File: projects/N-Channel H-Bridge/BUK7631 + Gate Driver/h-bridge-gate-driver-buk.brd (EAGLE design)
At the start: 160 x 100 mm, 24 parts, among them IC1 MIC5014YM, IC2 MIC5014YM, IC3 MIC5014YM, IC4 MIC5014YM, Q1 BUK7631, Q2 BUK7631, Q3 BUK7631, Q4 BUK7631'

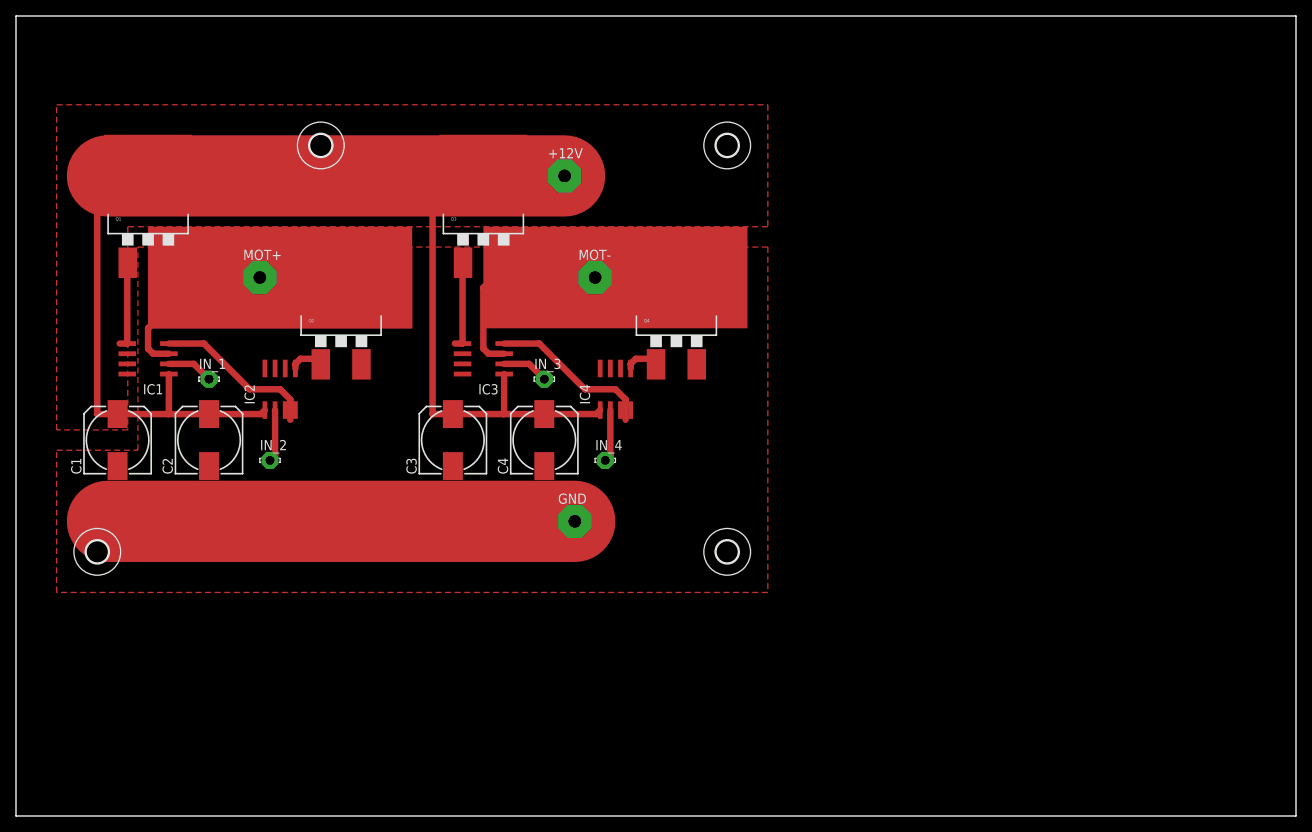
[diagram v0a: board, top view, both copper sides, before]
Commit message: smaller traces + images
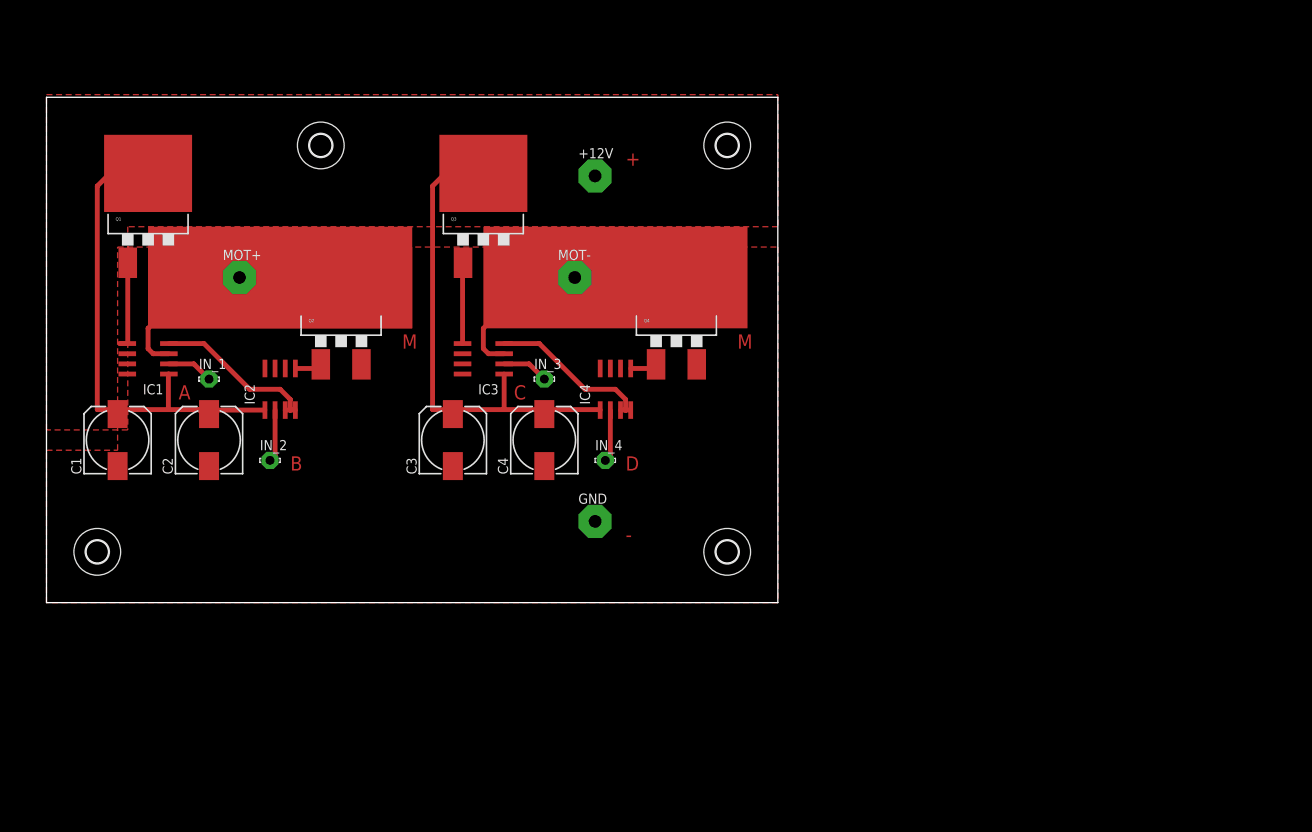
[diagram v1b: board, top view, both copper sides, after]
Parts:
- moved +12V 3.81 mm to (72.4, 80.0)
- moved GND 2.54 mm to (72.4, 36.8)
- moved MOT- 2.54 mm to (69.8, 67.3)
- moved MOT+ 2.54 mm to (27.9, 67.3)
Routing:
- net GND: track 99.6 -> 41.3 mm
- net VCC: track 174.1 -> 124.6 mm
- net N$4: track 11.1 -> 10.1 mm
- net MOT+: track 36.4 -> 37.1 mm
- net N$98: track 3.99 -> 3.39 mm
- net N$97: track 3.99 -> 3.39 mm
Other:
- board size 160 x 100 mm -> 91.4 x 63.2 mm
- board text added: "+"
- board text added: "-"
- board text added: "A"
- board text added: "B"
- board text added: "C"
- board text added: "D"
- board text added: "M"

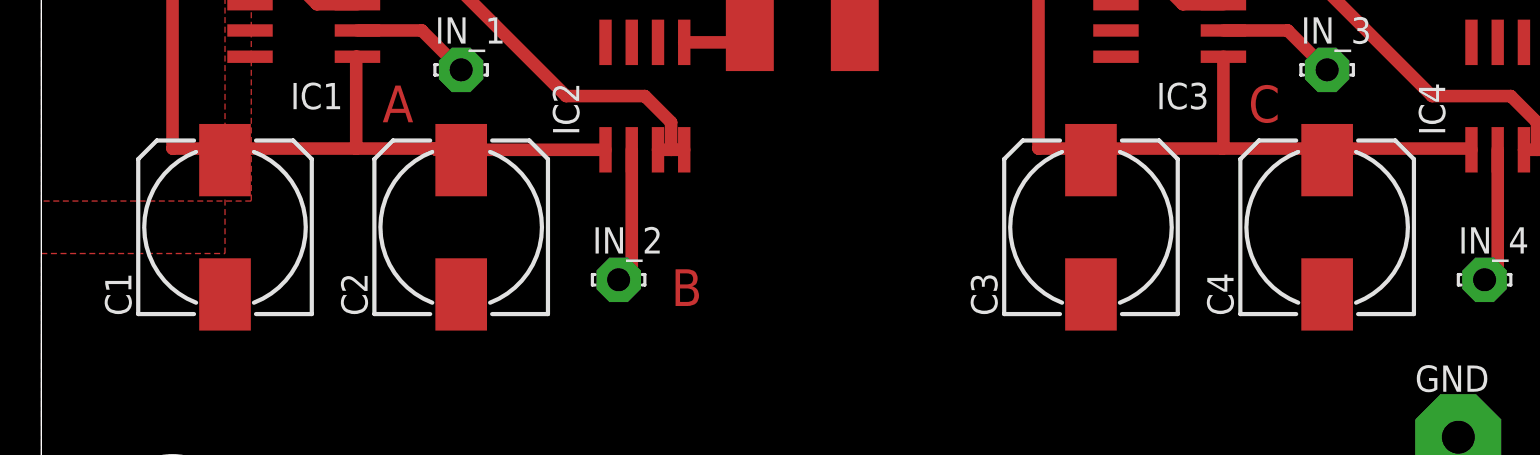
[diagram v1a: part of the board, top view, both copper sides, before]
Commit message: replaced with the proper cap package
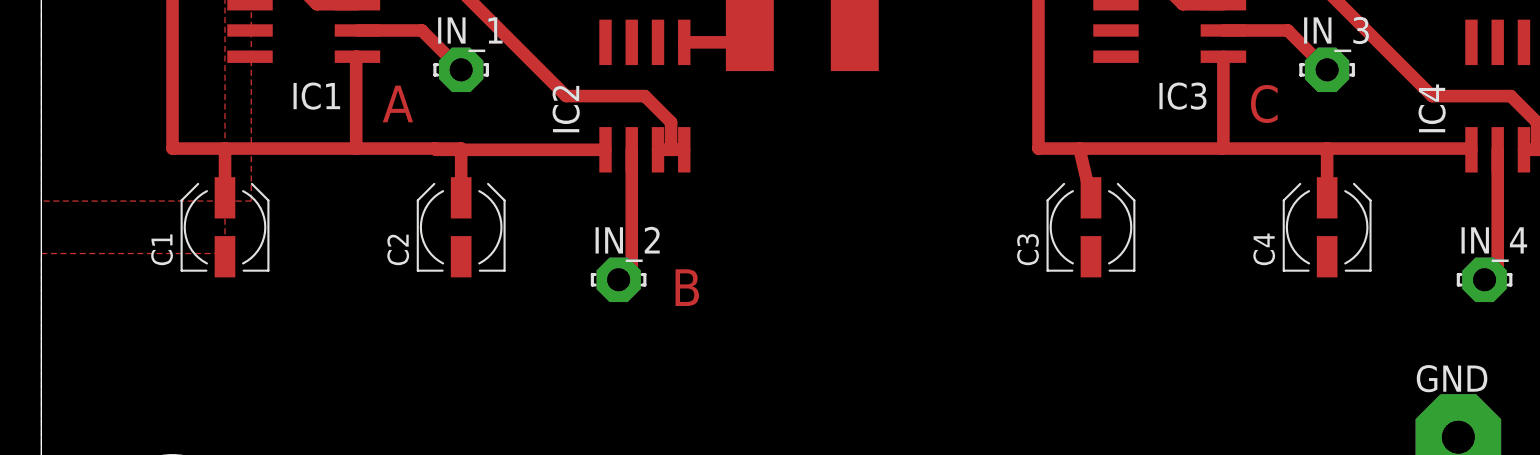
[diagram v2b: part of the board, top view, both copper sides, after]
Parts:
- C1, C2, C3, C4: device adafruit:153CLV-0810 -> rcl:UD-4X5,8_NICHICON
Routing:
- net VCC: track 124.6 -> 131.7 mm
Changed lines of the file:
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@@
 <elements>
 <element name="+12V" library="wirepad" package="4,16O1,6" value="" x="72.39" y="80.01"/>
-<element name="C1" library="adafruit" package="153CLV-0810" value="10uF" x="12.7" y="46.99" rot="R90"/>
-<element name="C2" library="adafruit" package="153CLV-0810" value="10uF" x="24.13" y="46.99" rot="R90"/>
-<element name="C3" library="adafruit" package="153CLV-0810" value="10uF" x="54.61" y="46.99" rot="R90"/>
-<element name="C4" library="adafruit" package="153CLV-0810" value="10uF" x="66.04" y="46.99" rot="R90"/>
+<element name="C1" library="rcl" package="UD-4X5,8_NICHICON" value="10uF" x="12.7" y="46.99" rot="R90"/>
+<element name="C2" library="rcl" package="UD-4X5,8_NICHICON" value="10uF" x="24.13" y="46.99" rot="R90"/>
+<element name="C3" library="rcl" package="UD-4X5,8_NICHICON" value="10uF" x="54.61" y="46.99" rot="R90"/>
+<element name="C4" library="rcl" package="UD-4X5,8_NICHICON" value="10uF" x="66.04" y="46.99" rot="R90"/>
 <element name="GND" library="wirepad" package="4,16O1,6" value="" x="72.39" y="36.83"/>
 <element name="IC1" library="nervus" package="SO8" value="MIC5014YM" x="16.51" y="57.15" rot="R90">
@@
 <wire x1="19.05" y1="55.245" x2="19.05" y2="50.8" width="0.6096" layer="1"/>
 <wire x1="19.05" y1="50.8" x2="12.7" y2="50.8" width="0.6096" layer="1"/>
-<wire x1="12.7" y1="50.8" x2="12.7" y2="50.24" width="0.6096" layer="1"/>
+<wire x1="12.7" y1="50.8" x2="12.7" y2="48.415" width="0.6096" layer="1"/>
 <wire x1="19.05" y1="50.8" x2="22.86" y2="50.8" width="0.6096" layer="1"/>
 <wire x1="22.86" y1="50.8" x2="24.13" y2="50.8" width="0.6096" layer="1"/>
-<wire x1="24.13" y1="50.8" x2="24.13" y2="50.24" width="0.6096" layer="1"/>
+<wire x1="24.13" y1="50.8" x2="24.13" y2="48.415" width="0.6096" layer="1"/>
 <wire x1="31.115" y1="50.74" x2="22.92" y2="50.74" width="0.6096" layer="1"/>
 <wire x1="22.92" y1="50.74" x2="22.86" y2="50.8" width="0.6096" layer="1"/>
@@
 <wire x1="52.07" y1="78.74" x2="52.07" y2="50.8" width="0.6096" layer="1"/>
 <wire x1="52.07" y1="50.8" x2="54.05" y2="50.8" width="0.6096" layer="1"/>
-<wire x1="54.05" y1="50.8" x2="54.61" y2="50.24" width="0.6096" layer="1"/>
+<wire x1="54.05" y1="50.8" x2="54.61" y2="48.415" width="0.6096" layer="1"/>
 <wire x1="54.05" y1="50.8" x2="60.96" y2="50.8" width="0.6096" layer="1"/>
 <wire x1="60.96" y1="50.8" x2="66.04" y2="50.8" width="0.6096" layer="1"/>
@@
 <wire x1="61.02" y1="55.245" x2="61.02" y2="50.86" width="0.6096" layer="1"/>
 <wire x1="61.02" y1="50.86" x2="60.96" y2="50.8" width="0.6096" layer="1"/>
-<wire x1="66.04" y1="50.24" x2="66.04" y2="50.8" width="0.6096" layer="1"/>
+<wire x1="66.04" y1="48.415" x2="66.04" y2="50.8" width="0.6096" layer="1"/>
 </signal>
 <signal name="N$98">

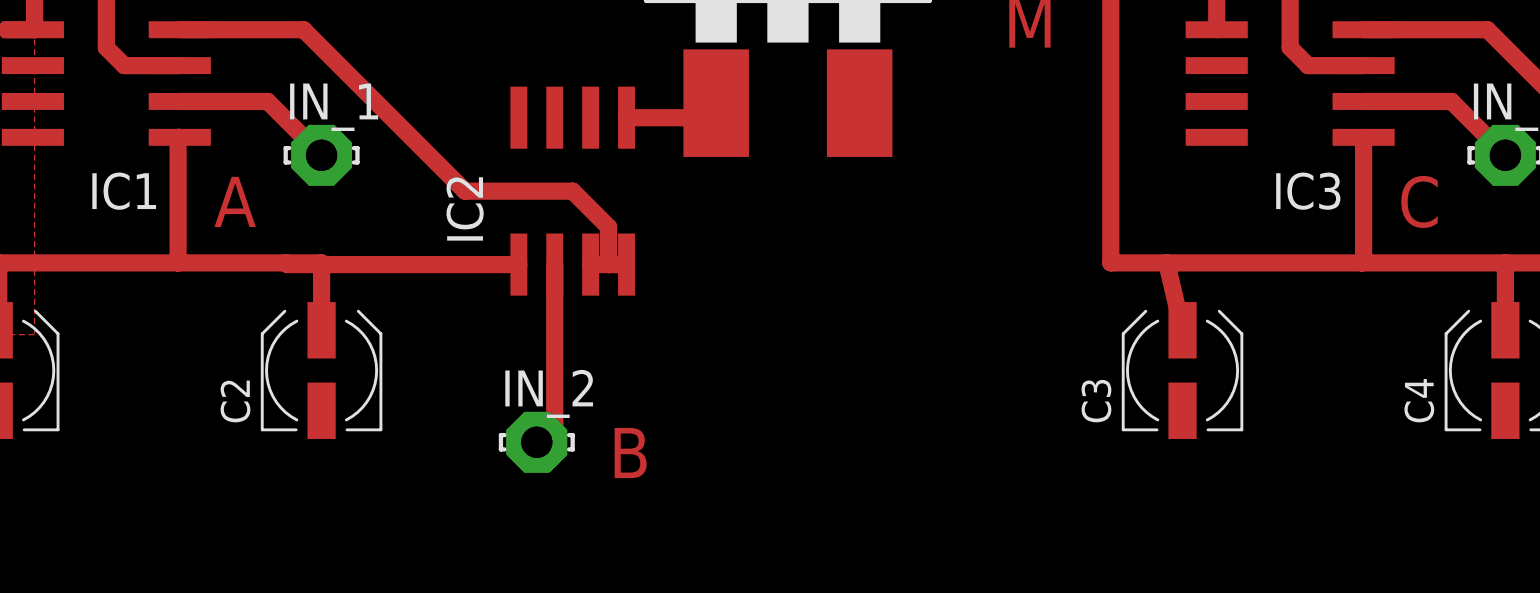
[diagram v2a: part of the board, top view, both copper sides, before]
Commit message: made nice traces for the caps
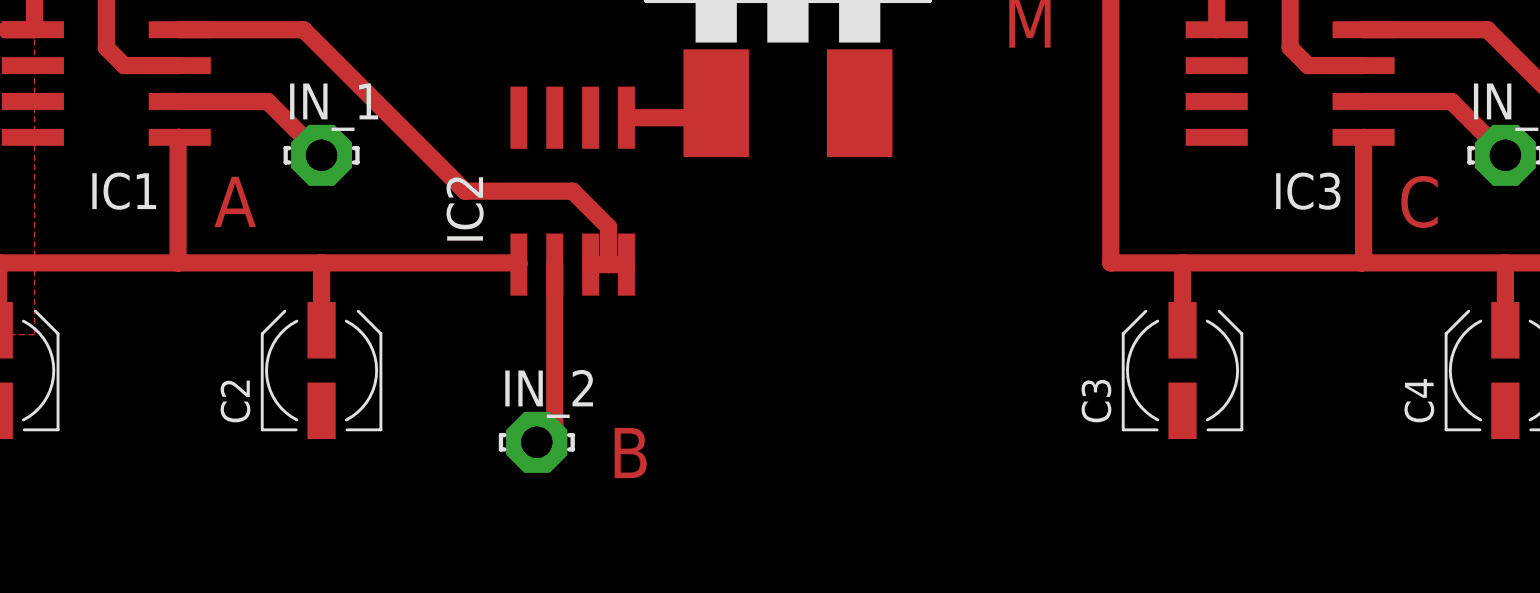
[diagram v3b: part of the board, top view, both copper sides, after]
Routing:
- net VCC: track 131.7 -> 130.4 mm
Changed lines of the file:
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@@
 <wire x1="19.05" y1="50.8" x2="12.7" y2="50.8" width="0.6096" layer="1"/>
 <wire x1="12.7" y1="50.8" x2="12.7" y2="48.415" width="0.6096" layer="1"/>
-<wire x1="19.05" y1="50.8" x2="22.86" y2="50.8" width="0.6096" layer="1"/>
-<wire x1="22.86" y1="50.8" x2="24.13" y2="50.8" width="0.6096" layer="1"/>
-<wire x1="24.13" y1="50.8" x2="24.13" y2="48.415" width="0.6096" layer="1"/>
-<wire x1="31.115" y1="50.74" x2="22.92" y2="50.74" width="0.6096" layer="1"/>
-<wire x1="22.92" y1="50.74" x2="22.86" y2="50.8" width="0.6096" layer="1"/>
 <wire x1="16.51" y1="80.325" x2="11.745" y2="80.325" width="0.6096" layer="1"/>
 <wire x1="11.745" y1="80.325" x2="10.16" y2="78.74" width="0.6096" layer="1"/>
@@
 <wire x1="53.655" y1="80.325" x2="52.07" y2="78.74" width="0.6096" layer="1"/>
 <wire x1="52.07" y1="78.74" x2="52.07" y2="50.8" width="0.6096" layer="1"/>
-<wire x1="52.07" y1="50.8" x2="54.05" y2="50.8" width="0.6096" layer="1"/>
-<wire x1="54.05" y1="50.8" x2="54.61" y2="48.415" width="0.6096" layer="1"/>
-<wire x1="54.05" y1="50.8" x2="60.96" y2="50.8" width="0.6096" layer="1"/>
+<wire x1="52.07" y1="50.8" x2="54.61" y2="50.8" width="0.6096" layer="1"/>
+<wire x1="54.61" y1="50.8" x2="60.96" y2="50.8" width="0.6096" layer="1"/>
 <wire x1="60.96" y1="50.8" x2="66.04" y2="50.8" width="0.6096" layer="1"/>
 <wire x1="66.04" y1="50.8" x2="72.965" y2="50.8" width="0.6096" layer="1"/>
@@
 <wire x1="61.02" y1="50.86" x2="60.96" y2="50.8" width="0.6096" layer="1"/>
 <wire x1="66.04" y1="48.415" x2="66.04" y2="50.8" width="0.6096" layer="1"/>
+<wire x1="54.61" y1="48.415" x2="54.61" y2="50.8" width="0.6096" layer="1"/>
+<wire x1="19.05" y1="50.8" x2="24.13" y2="50.8" width="0.6096" layer="1"/>
+<wire x1="24.13" y1="50.8" x2="31.115" y2="50.8" width="0.6096" layer="1"/>
+<wire x1="31.115" y1="50.8" x2="31.115" y2="50.74" width="0.6096" layer="1"/>
+<wire x1="24.13" y1="48.415" x2="24.13" y2="50.8" width="0.6096" layer="1"/>
 </signal>
 <signal name="N$98">
